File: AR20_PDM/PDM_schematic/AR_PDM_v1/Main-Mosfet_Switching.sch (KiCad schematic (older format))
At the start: 57 parts, among them SW1 SW_DIP_x07, U15 NMOS, U16 NMOS, U17 NMOS, U18 NMOS, U19 NMOS, U20 NMOS, U21 NMOS, U22 NMOS, U23 NMOS, U24 NMOS, U25 NMOS, U26 NMOS, U27 NMOS, U28 NMOS

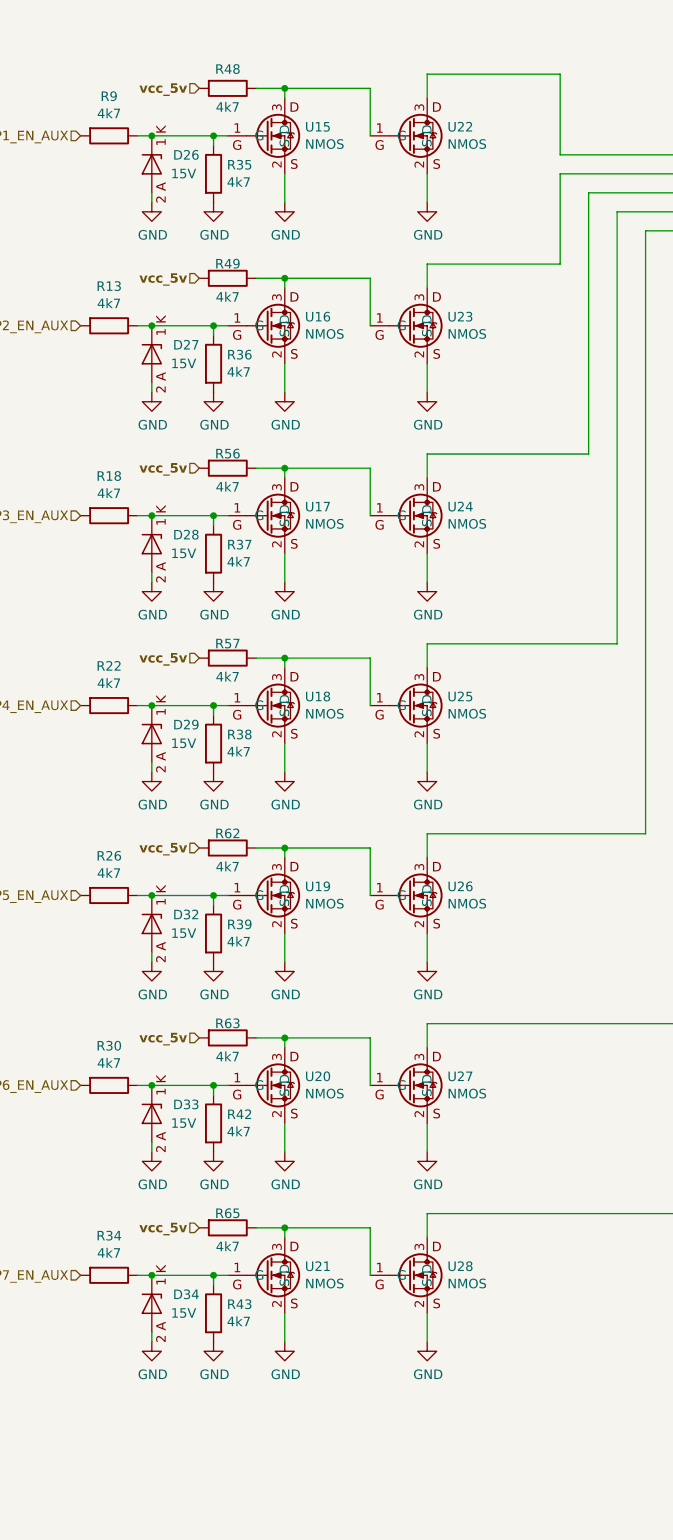
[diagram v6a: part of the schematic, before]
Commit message: shematics adjustments, and fixing values and names
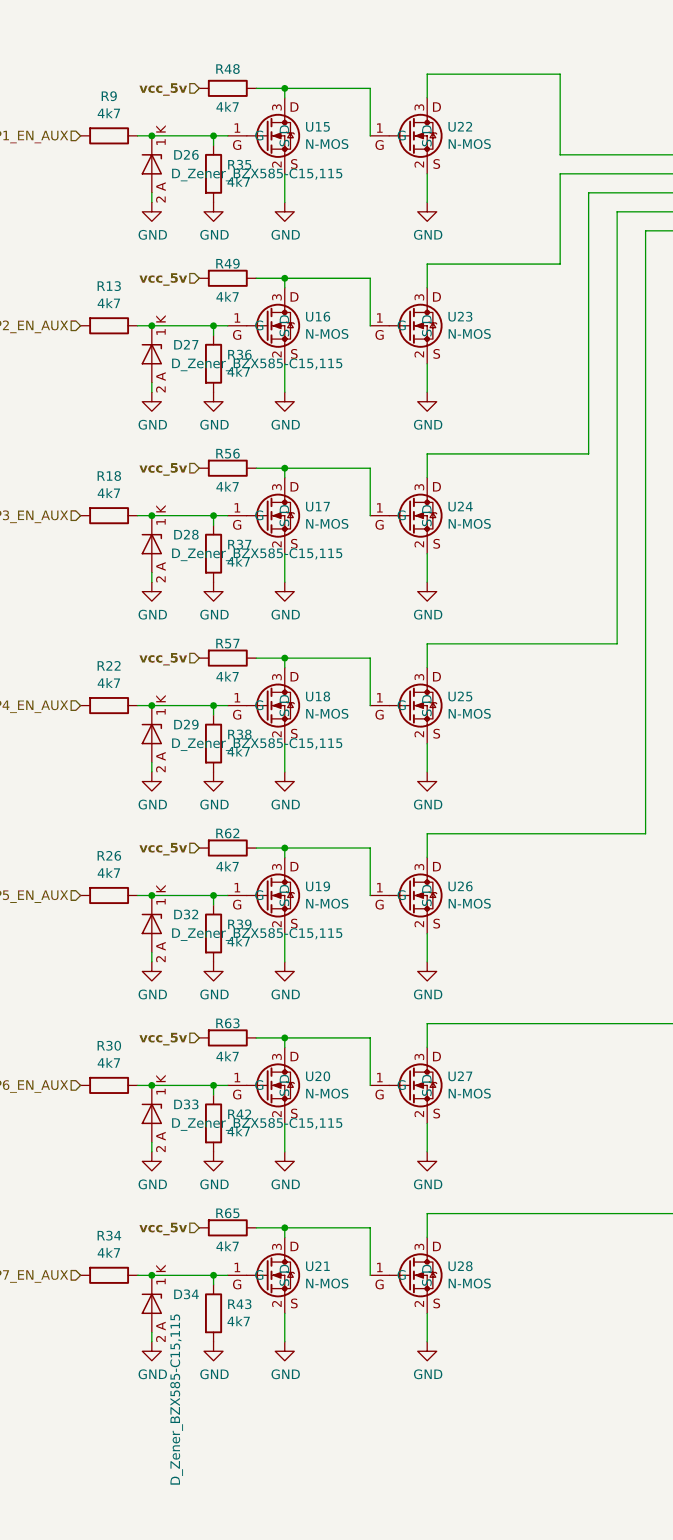
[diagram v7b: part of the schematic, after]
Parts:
- D26, D27, D28, D29, D32, D33, D34: value 15V -> D_Zener_BZX585-C15,115
- U15, U16, U17, U18, U19, U20, U21, U22, U23, U24, U25, U26, U27, U28: value NMOS -> N-MOS
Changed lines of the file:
@@
 AR Path="/5E683DA7/5E68C6B1" Ref="U15"  Part="1"
 F 0 "U15" H 2281 646 50  0000 L CNN
-F 1 "NMOS" H 2281 555 50  0000 L CNN
+F 1 "N-MOS" H 2281 555 50  0000 L CNN
 F 2 "AR_PDM_v1:N-MOS-DMN6140L-13" H 2175 1250 50  0001 C CNN
 F 3 "" H 2175 1250 50  0001 C CNN
@@
 AR Path="/5E683DA7/5E68F1FE" Ref="U22"  Part="1"
 F 0 "U22" H 3031 646 50  0000 L CNN
-F 1 "NMOS" H 3031 555 50  0000 L CNN
+F 1 "N-MOS" H 3031 555 50  0000 L CNN
 F 2 "AR_PDM_v1:N-MOS-DMN6140L-13" H 2925 1250 50  0001 C CNN
 F 3 "" H 2925 1250 50  0001 C CNN
@@
 P 1475 1150
 F 0 "D26" V 1427 1261 50  0000 L CNN
-F 1 "15V" V 1525 1250 50  0000 L CNN
+F 1 "D_Zener_BZX585-C15,115" V 1525 1250 50  0000 L CNN
 F 2 "AR_PDM_v1:Diode-BZX585-C15,115" H 1475 1150 50  0001 C CNN
 F 3 "" H 1475 1150 50  0001 C CNN
@@
 AR Path="/5E683DA7/5E6D8BBC" Ref="U16"  Part="1"
 F 0 "U16" H 2281 1646 50  0000 L CNN
-F 1 "NMOS" H 2281 1555 50  0000 L CNN
+F 1 "N-MOS" H 2281 1555 50  0000 L CNN
 F 2 "AR_PDM_v1:N-MOS-DMN6140L-13" H 2175 2250 50  0001 C CNN
 F 3 "" H 2175 2250 50  0001 C CNN
@@
 AR Path="/5E683DA7/5E6D8BD1" Ref="U23"  Part="1"
 F 0 "U23" H 3031 1646 50  0000 L CNN
-F 1 "NMOS" H 3031 1555 50  0000 L CNN
+F 1 "N-MOS" H 3031 1555 50  0000 L CNN
 F 2 "AR_PDM_v1:N-MOS-DMN6140L-13" H 2925 2250 50  0001 C CNN
 F 3 "" H 2925 2250 50  0001 C CNN
@@
 P 1475 2150
 F 0 "D27" V 1427 2261 50  0000 L CNN
-F 1 "15V" V 1525 2250 50  0000 L CNN
+F 1 "D_Zener_BZX585-C15,115" V 1525 2250 50  0000 L CNN
 F 2 "AR_PDM_v1:Diode-BZX585-C15,115" H 1475 2150 50  0001 C CNN
 F 3 "" H 1475 2150 50  0001 C CNN
@@
 AR Path="/5E683DA7/5E6EA1EE" Ref="U17"  Part="1"
 F 0 "U17" H 2281 2646 50  0000 L CNN
-F 1 "NMOS" H 2281 2555 50  0000 L CNN
+F 1 "N-MOS" H 2281 2555 50  0000 L CNN
 F 2 "AR_PDM_v1:N-MOS-DMN6140L-13" H 2175 3250 50  0001 C CNN
 F 3 "" H 2175 3250 50  0001 C CNN
@@
 AR Path="/5E683DA7/5E6EA203" Ref="U24"  Part="1"
 F 0 "U24" H 3031 2646 50  0000 L CNN
-F 1 "NMOS" H 3031 2555 50  0000 L CNN
+F 1 "N-MOS" H 3031 2555 50  0000 L CNN
 F 2 "AR_PDM_v1:N-MOS-DMN6140L-13" H 2925 3250 50  0001 C CNN
 F 3 "" H 2925 3250 50  0001 C CNN
@@
 P 1475 3150
 F 0 "D28" V 1427 3261 50  0000 L CNN
-F 1 "15V" V 1525 3250 50  0000 L CNN
+F 1 "D_Zener_BZX585-C15,115" V 1525 3250 50  0000 L CNN
 F 2 "AR_PDM_v1:Diode-BZX585-C15,115" H 1475 3150 50  0001 C CNN
 F 3 "" H 1475 3150 50  0001 C CNN
@@
 AR Path="/5E683DA7/5E6ED898" Ref="U18"  Part="1"
 F 0 "U18" H 2281 3646 50  0000 L CNN
-F 1 "NMOS" H 2281 3555 50  0000 L CNN
+F 1 "N-MOS" H 2281 3555 50  0000 L CNN
 F 2 "AR_PDM_v1:N-MOS-DMN6140L-13" H 2175 4250 50  0001 C CNN
 F 3 "" H 2175 4250 50  0001 C CNN
@@
 AR Path="/5E683DA7/5E6ED8AD" Ref="U25"  Part="1"
 F 0 "U25" H 3031 3646 50  0000 L CNN
-F 1 "NMOS" H 3031 3555 50  0000 L CNN
+F 1 "N-MOS" H 3031 3555 50  0000 L CNN
 F 2 "AR_PDM_v1:N-MOS-DMN6140L-13" H 2925 4250 50  0001 C CNN
 F 3 "" H 2925 4250 50  0001 C CNN
@@
 P 1475 4150
 F 0 "D29" V 1427 4261 50  0000 L CNN
-F 1 "15V" V 1525 4250 50  0000 L CNN
+F 1 "D_Zener_BZX585-C15,115" V 1525 4250 50  0000 L CNN
 F 2 "AR_PDM_v1:Diode-BZX585-C15,115" H 1475 4150 50  0001 C CNN
 F 3 "" H 1475 4150 50  0001 C CNN
@@
 AR Path="/5E683DA7/5E6F1B03" Ref="U19"  Part="1"
 F 0 "U19" H 2281 4646 50  0000 L CNN
-F 1 "NMOS" H 2281 4555 50  0000 L CNN
+F 1 "N-MOS" H 2281 4555 50  0000 L CNN
 F 2 "AR_PDM_v1:N-MOS-DMN6140L-13" H 2175 5250 50  0001 C CNN
 F 3 "" H 2175 5250 50  0001 C CNN
@@
 AR Path="/5E683DA7/5E6F1B18" Ref="U26"  Part="1"
 F 0 "U26" H 3031 4646 50  0000 L CNN
-F 1 "NMOS" H 3031 4555 50  0000 L CNN
+F 1 "N-MOS" H 3031 4555 50  0000 L CNN
 F 2 "AR_PDM_v1:N-MOS-DMN6140L-13" H 2925 5250 50  0001 C CNN
 F 3 "" H 2925 5250 50  0001 C CNN
@@
 P 1475 5150
 F 0 "D32" V 1427 5261 50  0000 L CNN
-F 1 "15V" V 1525 5250 50  0000 L CNN
+F 1 "D_Zener_BZX585-C15,115" V 1525 5250 50  0000 L CNN
 F 2 "AR_PDM_v1:Diode-BZX585-C15,115" H 1475 5150 50  0001 C CNN
 F 3 "" H 1475 5150 50  0001 C CNN
@@
 AR Path="/5E683DA7/5E6F6D96" Ref="U20"  Part="1"
 F 0 "U20" H 2281 5646 50  0000 L CNN
-F 1 "NMOS" H 2281 5555 50  0000 L CNN
+F 1 "N-MOS" H 2281 5555 50  0000 L CNN
 F 2 "AR_PDM_v1:N-MOS-DMN6140L-13" H 2175 6250 50  0001 C CNN
 F 3 "" H 2175 6250 50  0001 C CNN
@@
 AR Path="/5E683DA7/5E6F6DAB" Ref="U27"  Part="1"
 F 0 "U27" H 3031 5646 50  0000 L CNN
-F 1 "NMOS" H 3031 5555 50  0000 L CNN
+F 1 "N-MOS" H 3031 5555 50  0000 L CNN
 F 2 "AR_PDM_v1:N-MOS-DMN6140L-13" H 2925 6250 50  0001 C CNN
 F 3 "" H 2925 6250 50  0001 C CNN
@@
 P 1475 6150
 F 0 "D33" V 1427 6261 50  0000 L CNN
-F 1 "15V" V 1525 6250 50  0000 L CNN
+F 1 "D_Zener_BZX585-C15,115" V 1525 6250 50  0000 L CNN
 F 2 "AR_PDM_v1:Diode-BZX585-C15,115" H 1475 6150 50  0001 C CNN
 F 3 "" H 1475 6150 50  0001 C CNN
@@
 AR Path="/5E683DA7/5E6FAF62" Ref="U21"  Part="1"
 F 0 "U21" H 2281 6646 50  0000 L CNN
-F 1 "NMOS" H 2281 6555 50  0000 L CNN
+F 1 "N-MOS" H 2281 6555 50  0000 L CNN
 F 2 "AR_PDM_v1:N-MOS-DMN6140L-13" H 2175 7250 50  0001 C CNN
 F 3 "" H 2175 7250 50  0001 C CNN
@@
 AR Path="/5E683DA7/5E6FAF77" Ref="U28"  Part="1"
 F 0 "U28" H 3031 6646 50  0000 L CNN
-F 1 "NMOS" H 3031 6555 50  0000 L CNN
+F 1 "N-MOS" H 3031 6555 50  0000 L CNN
 F 2 "AR_PDM_v1:N-MOS-DMN6140L-13" H 2925 7250 50  0001 C CNN
 F 3 "" H 2925 7250 50  0001 C CNN
@@
 P 1475 7150
 F 0 "D34" V 1427 7261 50  0000 L CNN
-F 1 "15V" V 1525 7250 50  0000 L CNN
+F 1 "D_Zener_BZX585-C15,115" H 1525 7275 50  0000 L CNN
 F 2 "AR_PDM_v1:Diode-BZX585-C15,115" H 1475 7150 50  0001 C CNN
 F 3 "" H 1475 7150 50  0001 C CNN
